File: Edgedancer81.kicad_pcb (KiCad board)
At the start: 2 copper layers, 355.6 x 124.6 mm, 181 parts, among them SW1 SW_Push, SW2 Rotary_Encoder_Switch, U1 ATmega32U4-AU, Y1 16MHz

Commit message: Updated for type-c
Still needs to update the pcb
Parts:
- added F1: 500mA, Fuse:Fuse_1206_3216Metric, B.Cu at (282.6, 50.0)
- added R5: 5k1, Resistor_SMD:R_0805_2012Metric, B.Cu at (282.0, 46.9)
- added R6: 5k1, Resistor_SMD:R_0805_2012Metric, B.Cu at (287.6, 50.2)
- added R7: 22, Resistor_SMD:R_0805_2012Metric, B.Cu at (282.0, 43.9)
- added R8: 22, Resistor_SMD:R_0805_2012Metric, B.Cu at (286.4, 46.9)
- added U2: PRTR5V0U2X, random-keyboard-parts:SOT143B, B.Cu at (286.2, 43.4)
- added USB1: HRO-TYPE-C-31-M-12, Type-C:HRO-TYPE-C-31-M-12-Assembly, B.Cu at (320.7, 56.4)

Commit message: Finished traces
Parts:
- removed the F1 at (317.5, 111.6)
- removed R1, R2: 22, Resistor_SMD:R_0805_2012Metric
- removed the USB1 at (320.7, 77.0)
- moved R7 83.1 mm to (319.1, 118.3), turned to 90 degrees
- moved R8 79.5 mm to (321.5, 118.3), turned to 90 degrees
- moved U2 52.5 mm to (320.3, 83.3), turned to 180 degrees
- moved F1 52.2 mm to (318.1, 88.3), turned to 90 degrees
- moved R5 50.4 mm to (316.7, 83.3), turned to 90 degrees
- moved R6 50.3 mm to (325.4, 83.3), turned to 90 degrees
- moved USB1 14.3 mm to (320.7, 70.6)
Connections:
- U1 pad 3: Net-(R1-Pad2) -> D-
- U1 pad 4: Net-(R2-Pad2) -> D+
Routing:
- net Net-(R8-Pad2): track 0.00 -> 43.5 mm
- net Net-(R7-Pad2): track 0.00 -> 42.4 mm
- net Net-(R1-Pad2): track 35.1 -> 0.00 mm
- net GND: track 186.6 -> 221.4 mm
- net Net-(R2-Pad2): track 33.9 -> 0.00 mm
- net +5V: track 144.7 -> 169.5 mm
- net VCC: track 29.4 -> 15.6 mm, vias 0 -> 2
- net Net-(R6-Pad2): track 0.00 -> 6.25 mm, vias 0 -> 2
- net Net-(R5-Pad2): track 0.00 -> 6.12 mm, vias 0 -> 2
- net D+: track 36.2 -> 33.9 mm
- net D-: track 36.5 -> 35.1 mm
- removed copper zone on F.Cu, net GND
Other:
- board size 355.6 x 124.6 mm -> 355.6 x 127.1 mm

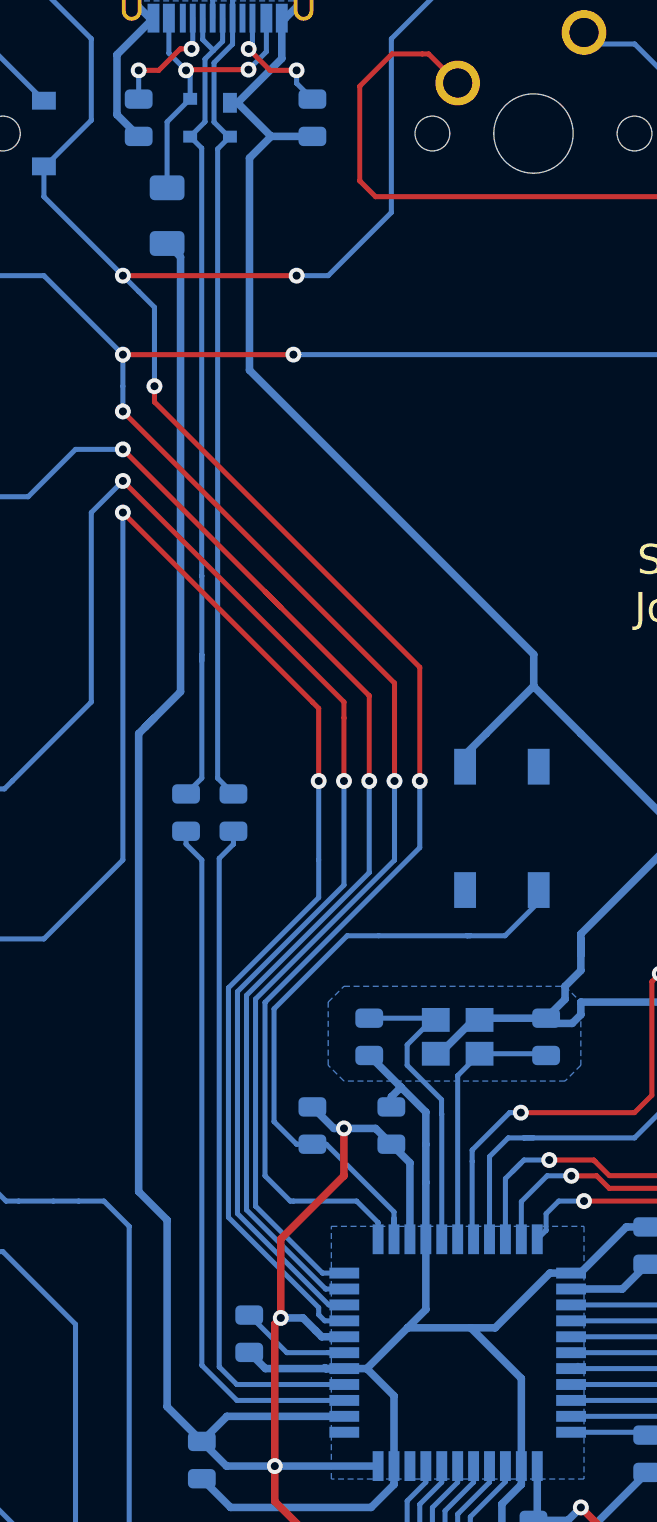
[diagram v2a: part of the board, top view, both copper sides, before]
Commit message: cleaned up data traces
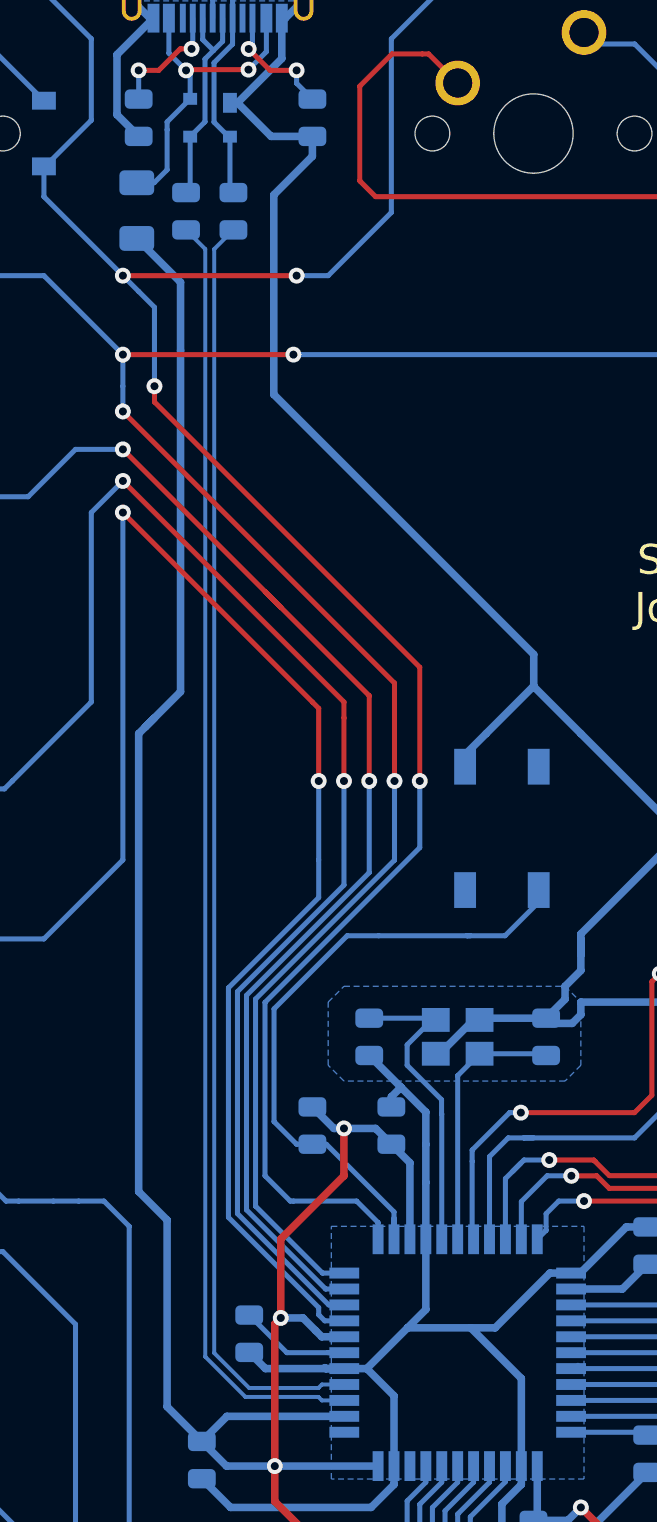
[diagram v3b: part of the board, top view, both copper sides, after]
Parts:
- moved R7 30.2 mm to (319.1, 88.0)
- moved R8 30.2 mm to (321.5, 88.0)
- moved F1 1.55 mm to (316.6, 88.0)
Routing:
- net Net-(R7-Pad2): track 42.4 -> 11.4 mm
- net Net-(R8-Pad2): track 43.5 -> 12.8 mm
- net D+: track 33.9 -> 64.2 mm
- net D-: track 35.1 -> 64.9 mm
- net VCC: track 15.6 -> 16.5 mm
- net +5V: track 169.5 -> 170.4 mm
